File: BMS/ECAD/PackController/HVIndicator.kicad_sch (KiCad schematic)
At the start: 35 parts, among them U1 Viper26K

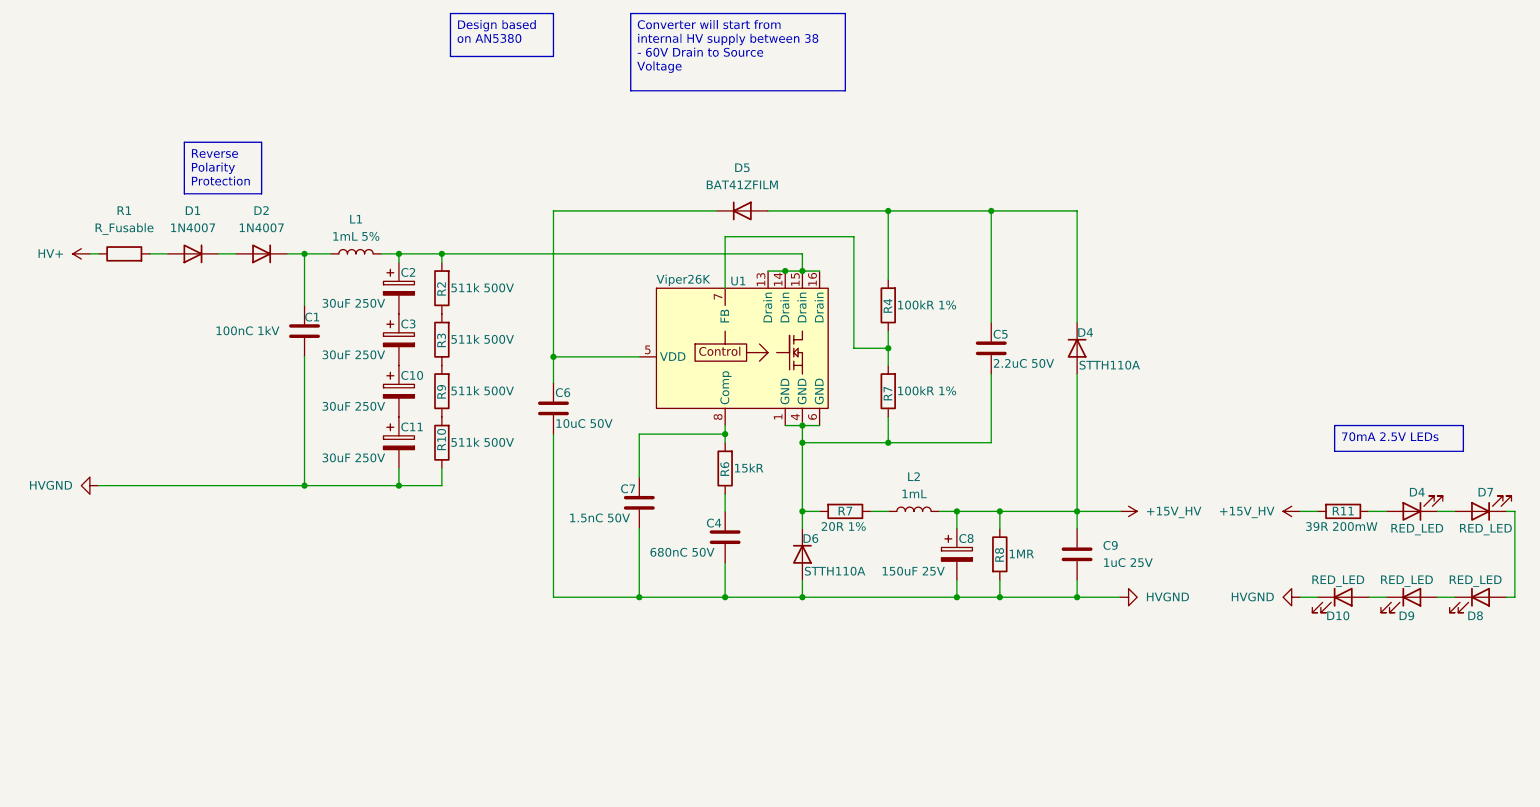
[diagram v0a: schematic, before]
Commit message: did AIR monitoring circuit and started SDC CTRL / logik
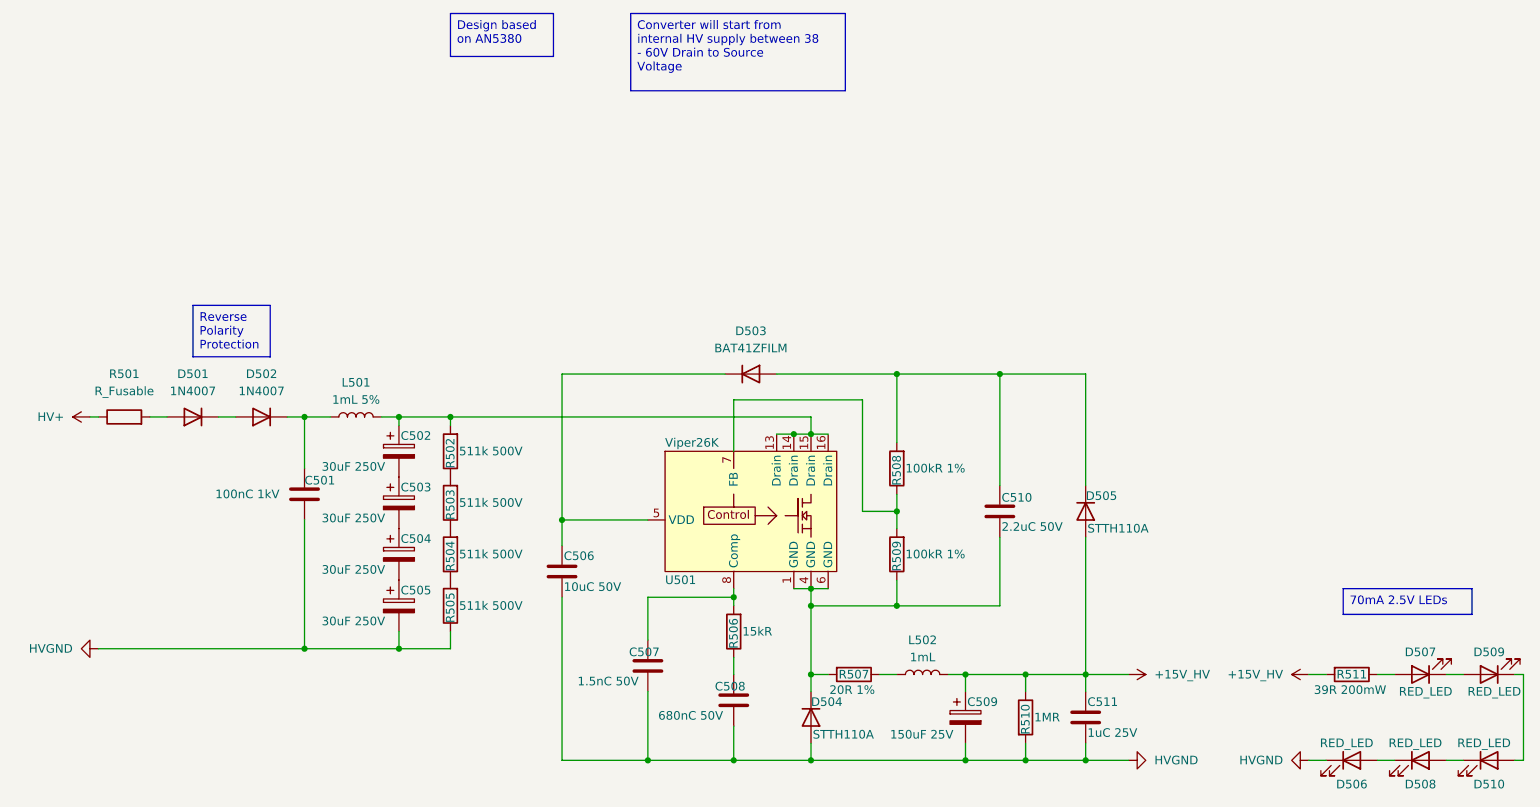
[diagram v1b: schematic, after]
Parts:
- renumbered C1 to C501, C2 to C502, C3 to C503, C10 to C504, C11 to C505, C6 to C506, C7 to C507, C4 to C508, C8 to C509, C5 to C510, C9 to C511, D1 to D501, D2 to D502, D5 to D503, D6 to D504, D4 to D505, D10 to D506, D4 to D507, D9 to D508, D7 to D509, D8 to D510, L1 to L501, L2 to L502, R1 to R501, R2 to R502, R3 to R503, R9 to R504, R10 to R505, R6 to R506, R7 to R507, R4 to R508, R7 to R509, R8 to R510, R11 to R511, U1 to U501
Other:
- moved on the sheet: C501, C502, C503, C504, C505, C506, C507, C508, C509, C510, C511, D501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

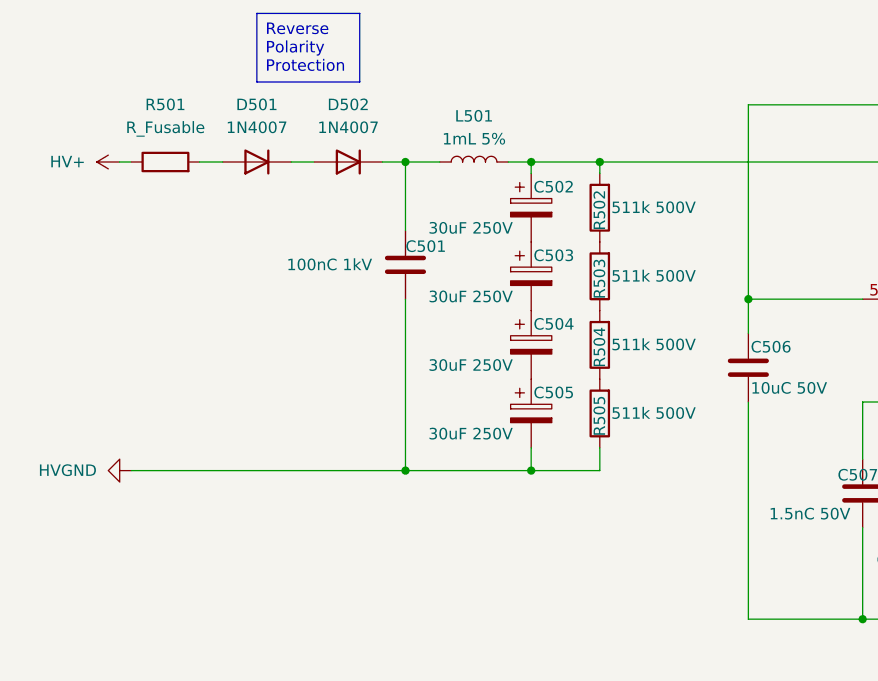
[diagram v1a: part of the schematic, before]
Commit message: IMD control circuit
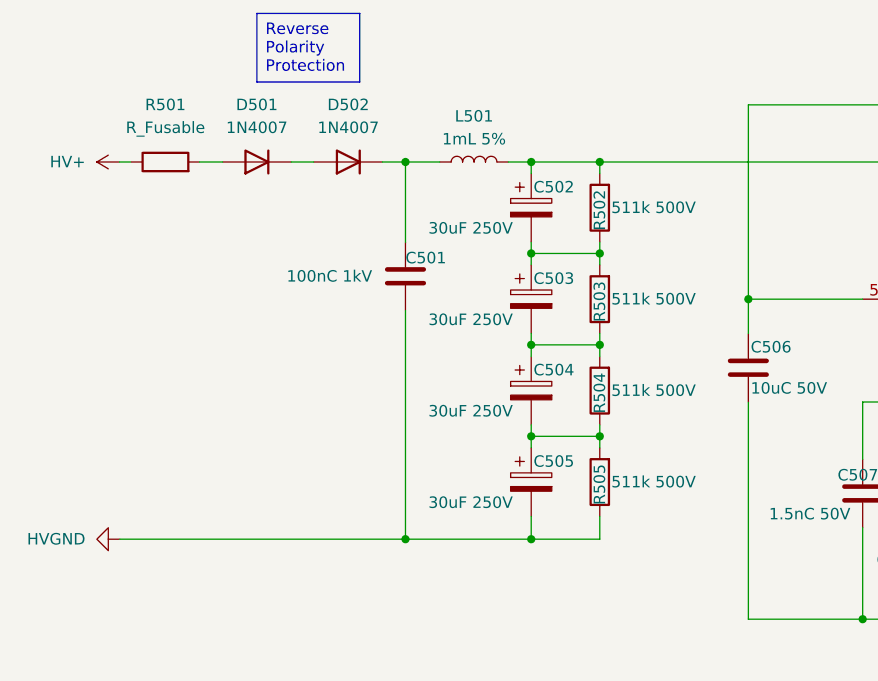
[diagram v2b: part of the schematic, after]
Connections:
- net at R504.1, R505.2: now also C504.2, C505.1
- net at R503.1, R504.2: now also C503.2, C504.1
- net at R502.1, R503.2: now also C502.2, C503.1
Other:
- moved on the sheet: C501, C503, C504, C505, R503, R504, R505
